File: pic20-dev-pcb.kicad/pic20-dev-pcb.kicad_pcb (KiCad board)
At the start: 2 copper layers, 41.5 x 40.1 mm, 21 parts, among them J1 PGM-Conn, J2 App_Conn_1, J3 App_Conn_2, J4 Conn_SR, J5 Conn_01x03_Male, J6 Conn_BB1, J7 Conn_01x03_Male, SW1 SW_Push, U1 PIC16F1829-IP, U2 TLV1117-33

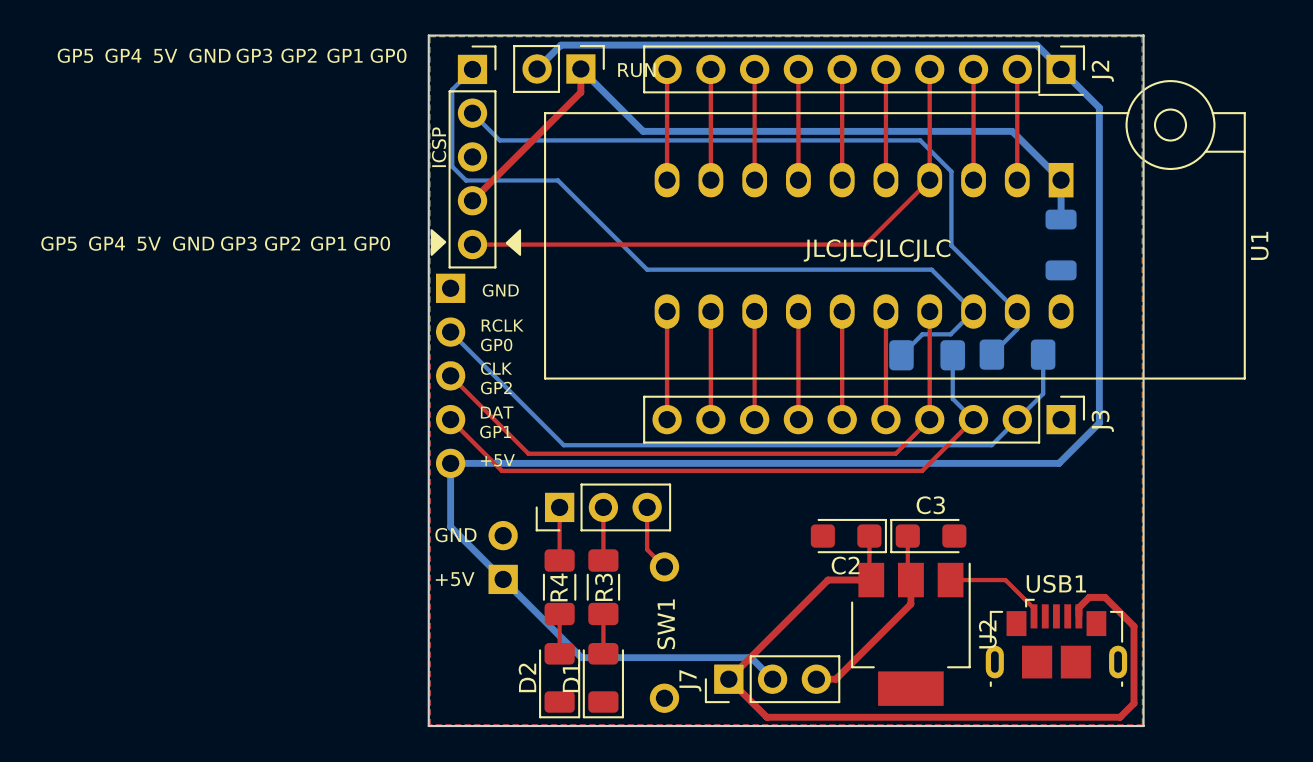
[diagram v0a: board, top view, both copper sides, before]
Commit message: pic20-dev-pcb: Rev 1.2: use DIP-20 footprint for PIC
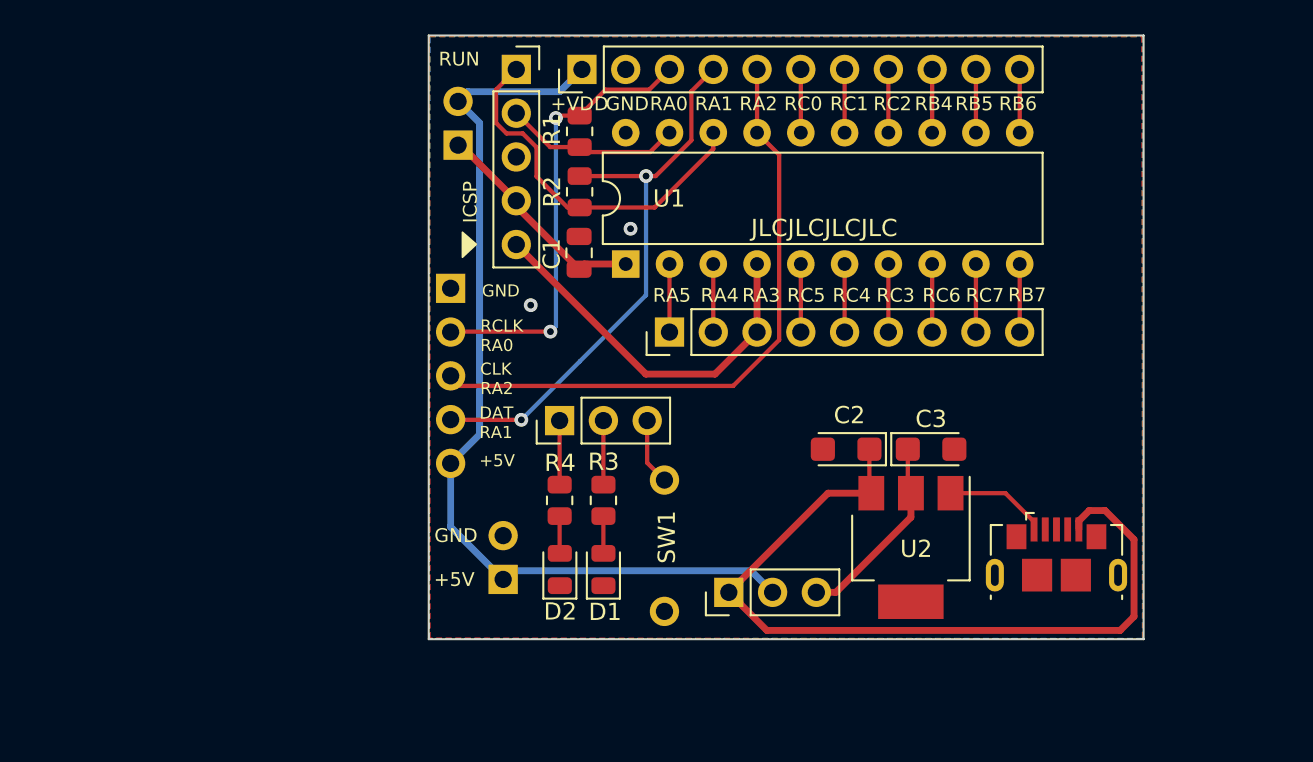
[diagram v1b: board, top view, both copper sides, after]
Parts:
- C1: footprint Capacitor_SMD:C_1206_3216Metric -> Capacitor_SMD:C_0805_2012Metric; moved to F.Cu
- D1, D2: footprint LED_SMD:LED_1206_3216Metric -> LED_SMD:LED_0805_2012Metric
- J2: footprint Connector_PinHeader_2.54mm:PinHeader_1x10_P2.54mm_Vertical -> Connector_PinHeader_2.54mm:PinHeader_1x09_P2.54mm_Vertical
- J3: footprint Connector_PinHeader_2.54mm:PinHeader_1x10_P2.54mm_Vertical -> Connector_PinHeader_2.54mm:PinHeader_1x11_P2.54mm_Vertical
- JP1: moved to B.Cu
- R1, R2: footprint Resistor_SMD:R_1206_3216Metric_Pad1.42x1.75mm_HandSolder -> Resistor_SMD:R_0805_2012Metric; moved to F.Cu
- R3, R4: footprint Resistor_SMD:R_1206_3216Metric_Pad1.30x1.75mm_HandSolder -> Resistor_SMD:R_0805_2012Metric
- U1: footprint Socket:DIP_Socket-20_W4.3_W5.08_W7.62_W10.16_W10.9_3M_220-3342-00-0602J -> Package_DIP:DIP-20_W7.62mm
- moved J3 34.4 mm to (105.4, 76.2), turned to 90 degrees
- moved R1 28.5 mm to (105.3, 79.8), turned to 90 degrees
- moved C1 28.0 mm to (105.2, 86.8), turned to 270 degrees
- moved J2 27.4 mm to (110.5, 91.4), turned to 90 degrees
- moved U1 25.7 mm to (108.0, 87.5), turned to 90 degrees
- moved R2 22.3 mm to (105.3, 83.3), turned to 90 degrees
- moved JP1 8.38 mm to (98.2, 80.6), turned to 0 degrees
- moved D2 6.29 mm to (104.1, 105.2)
- moved D1 6.29 mm to (106.7, 105.2)
- moved J5 5.04 mm to (104.1, 96.6)
- moved J7 5.04 mm to (113.9, 106.5)
- moved U2 5.04 mm to (124.5, 103.9)
- moved C2 5.04 mm to (120.7, 98.2)
- moved C3 5.04 mm to (125.7, 98.2)
- moved R3 5.04 mm to (106.7, 101.2)
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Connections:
- J2 pad 1: /+VDD -> /RA5
- J2 pad 2: /RA5 -> /RA4
- J2 pad 3: /RA4 -> /RA3
- J2 pad 4: /RA3 -> /RC5
- J2 pad 5: /RC5 -> /RC4
- J2 pad 6: /RC4 -> /RC3
- J2 pad 7: /RC3 -> /RC6
- J2 pad 8: /RC6 -> /RC7
- J2 pad 9: /RC7 -> /RB7
- J3 pad 1: GND -> /+VDD
- J3 pad 10: /RB6 -> /RB5
- J3 pad 2: /RA0 -> GND
- J3 pad 3: /RA1 -> /RA0
- J3 pad 4: /RA2 -> /RA1
- J3 pad 5: /RC0 -> /RA2
- J3 pad 6: /RC1 -> /RC0
- J3 pad 7: /RC2 -> /RC1
- J3 pad 8: /RB4 -> /RC2
- J3 pad 9: /RB5 -> /RB4
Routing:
- net /+VDD: track 117.6 -> 54.5 mm
- net Net-(J1-Pad2): track 42.0 -> 10.3 mm
- net Net-(C1-Pad2): track 43.1 -> 13.0 mm
- net Net-(J1-Pad1): track 45.1 -> 21.6 mm
- net /RA0: track 40.6 -> 26.1 mm, vias 0 -> 2
- net /RA3: track 34.5 -> 22.0 mm
- net /RA1: track 37.0 -> 33.8 mm, vias 0 -> 2
- net /RC2: track 6.27 -> 3.67 mm
- net /RC1: track 6.27 -> 3.67 mm
- net /RC0: track 6.27 -> 3.67 mm
- net /RB6: track 6.27 -> 3.67 mm
- net /RB5: track 6.27 -> 3.67 mm
- net /RB4: track 6.27 -> 3.67 mm
- net /RC7: track 6.43 -> 3.95 mm
- net /RC6: track 6.43 -> 3.95 mm
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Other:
- board size 41.5 x 40.1 mm -> 41.5 x 35 mm
- board text added: "+VDD"
- board text added: "CLK RA2"
- board text added: "DAT RA1"
- board text added: "RA0"
- board text added: "RA1"
- board text added: "RA2"
- board text added: "RA3"
- board text added: "RA4"
- board text added: "RA5"
- board text added: "RB4"
- board text added: "RB5"
- board text added: "RB6"
- board text added: "RB7"
- board text added: "RC0"
- board text added: "RC1"
- board text added: "RC2"
- board text added: "RC3"
- board text added: "RC4"
- board text added: "RC5"
- board text added: "RC6"
- board text added: "RC7"
- board text added: "RCLK RA0"
- board text added: "Rev 1.2"
- board text removed: "5V"
- board text removed: "CLK GP2"
- board text removed: "DAT GP1"
- board text removed: "GP0"
- board text removed: "GP1"
- board text removed: "GP2"
- board text removed: "GP3"
- board text removed: "GP4"
- board text removed: "GP5"
- board text removed: "RCLK GP0"
- board text removed: "Rev 6"
- board text removed: "f"

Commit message: pic20-dev-pcb: Rev 1.3: add SPI-connector, use socket for PIC
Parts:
- added J8: SPI_Conn, Connector_PinHeader_2.54mm:PinHeader_1x06_P2.54mm_Vertical, F.Cu at (134.6, 76.2)
- U1: footprint Package_DIP:DIP-20_W7.62mm -> Package_DIP:DIP-20_W7.62mm_Socket
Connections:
- net /RB6 renamed /CLK
- net /RC6 renamed /CS
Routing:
- net /+VDD: track 54.5 -> 84.7 mm
- net /RB4: track 3.67 -> 15.2 mm
- net /CS: track 3.95 -> 15.4 mm
- net /RC7: track 3.95 -> 12.6 mm
- net /CLK: track 3.67 -> 9.41 mm
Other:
- board text added: "CLK"
- board text added: "CS"
- board text added: "Rev 1.3"
- board text added: "SDI"
- board text added: "SDO"
- board text added: "Vdd"
- board text removed: "+VDD"
- board text removed: "Rev 1.2"

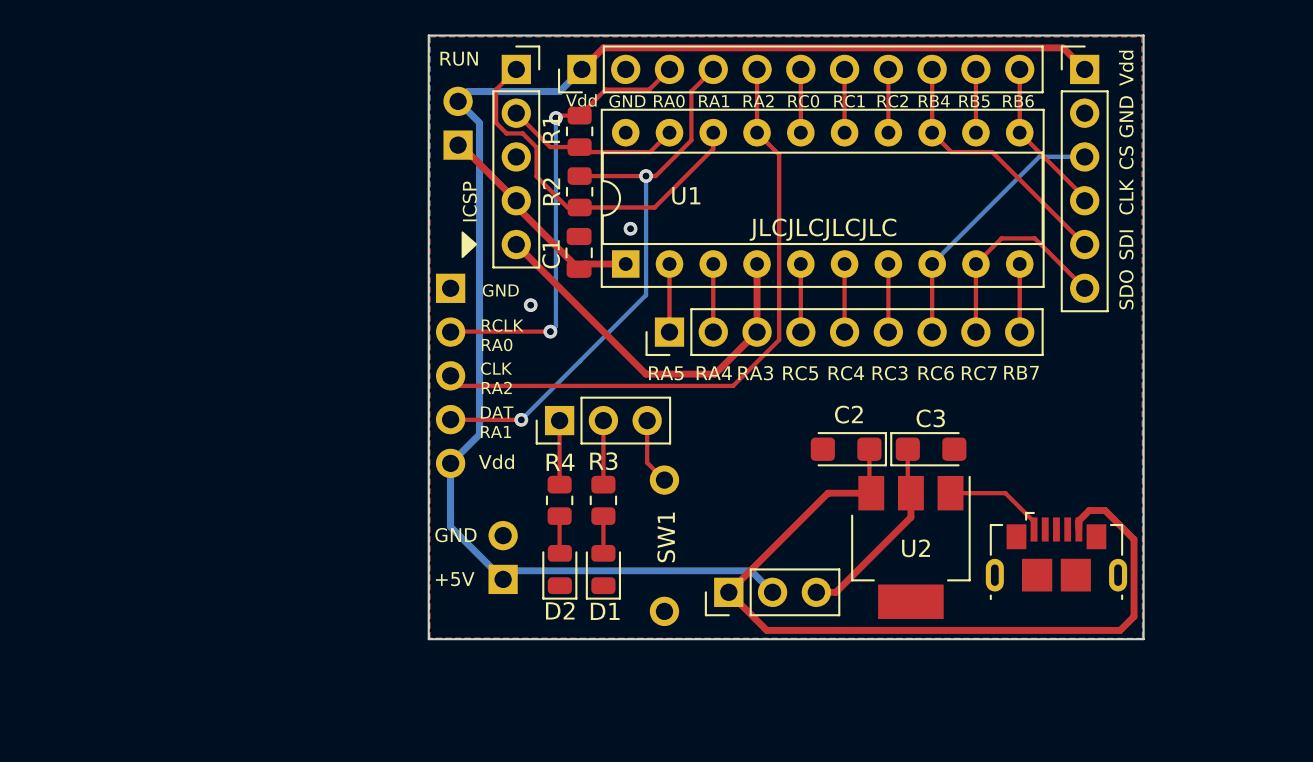
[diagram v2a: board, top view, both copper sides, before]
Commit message: updated footprint for micro-usb
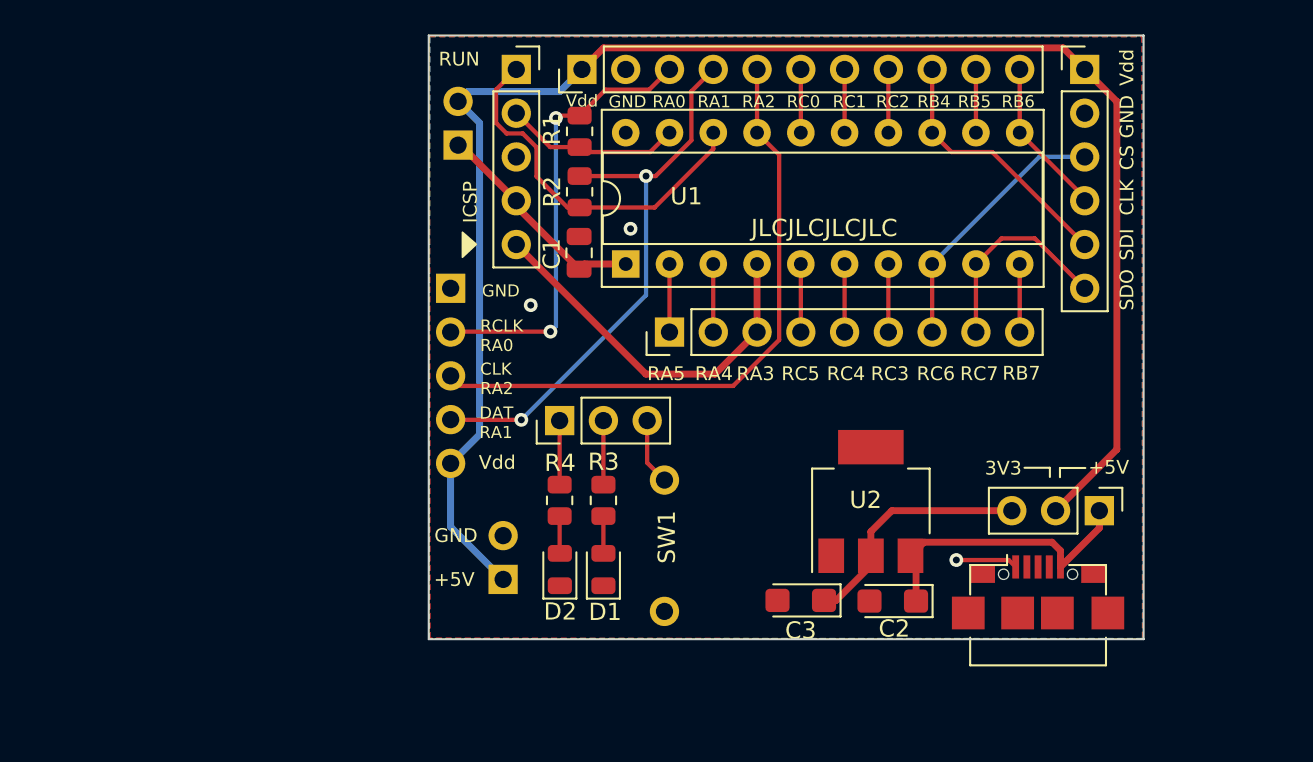
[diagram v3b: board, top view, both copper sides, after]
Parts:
- USB1: footprint Connector_USB:USB_Micro-B_GCT_USB3076-30-A -> user:USB_Micro-B_JLCPCB_40942
- moved J7 22.0 mm to (135.4, 101.8), turned to 270 degrees
- moved C3 11.6 mm to (118.1, 107.0), turned to 180 degrees
- moved C2 9.22 mm to (123.4, 107.0)
- moved U2 3.54 mm to (122.2, 101.3), turned to 90 degrees
- moved USB1 1.29 mm to (131.9, 105.1)
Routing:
- net Net-(C2-Pad1): track 47.1 -> 17.1 mm
- net /+VDD: track 84.7 -> 96.9 mm
- net Net-(C3-Pad1): track 11.5 -> 14.2 mm
- net GND: track 5.98 -> 3.61 mm, vias 2 -> 3
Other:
- board text added: "3V3"
- board text removed: "+"
- board text removed: "-"

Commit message: optimized layout
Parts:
- J4: moved to F.Cu
- moved U2 1.52 mm to (122.0, 99.8)
- moved C2 1.52 mm to (123.3, 105.5)
- moved C3 1.52 mm to (118.0, 105.5)
- moved C1 0.50 mm to (105.2, 87.3)
- moved R2 0.36 mm to (105.1, 83.6)
- moved R1 0.15 mm to (105.1, 79.8)
- turned J4 to 0 degrees
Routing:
- net GND: track 3.61 -> 6.96 mm
- net Net-(C1-Pad2): track 13.0 -> 14.1 mm
- net /RA3: track 22.0 -> 22.7 mm

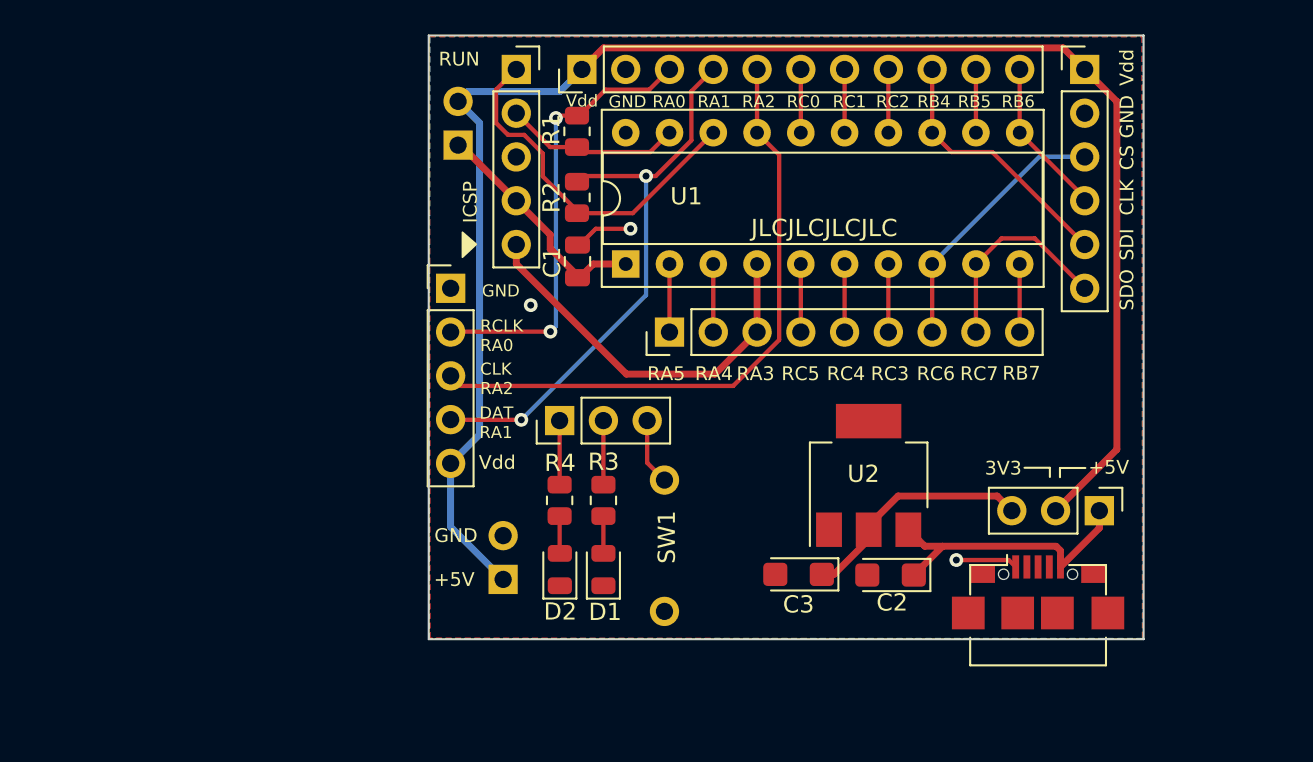
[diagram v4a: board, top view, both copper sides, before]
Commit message: pic20-dev-pcb: Rev 1.4: optimizations, prep for production
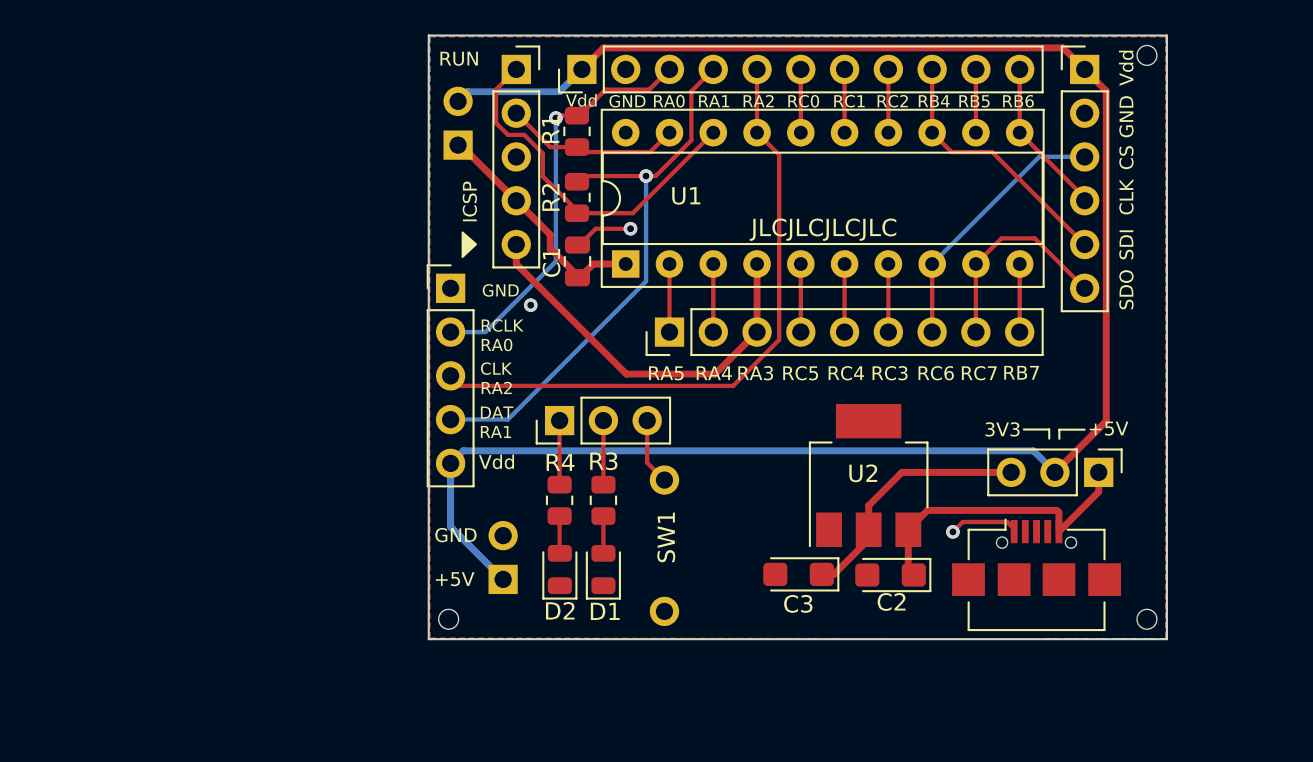
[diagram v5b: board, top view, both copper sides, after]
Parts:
- added REF**: SMT_JLCPCB_ToolingHole, user:SMT_JLCPCB_ToolingHole, F.Cu at (138.2, 108.1)
- added REF**: SMT_JLCPCB_ToolingHole, user:SMT_JLCPCB_ToolingHole, F.Cu at (97.7, 108.1)
- added REF**: SMT_JLCPCB_ToolingHole, user:SMT_JLCPCB_ToolingHole, F.Cu at (138.2, 75.4)
- D1: value LED -> LED yellow
- D2: value LED -> LED red
- R3, R4: value 1kΩ -> 1K
- moved J7 2.22 mm to (135.4, 99.6)
- moved USB1 0.66 mm to (131.8, 104.4)
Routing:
- net /+VDD: track 96.9 -> 107.9 mm
- net /RA0: track 26.1 -> 23.9 mm, vias 2 -> 1
- net Net-(C3-Pad1): track 13.7 -> 14.8 mm
- net /RA1: track 34.0 -> 33.4 mm, vias 2 -> 1
- net Net-(C2-Pad1): track 16.8 -> 17.4 mm
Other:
- board size 41.5 x 35 mm -> 42.8 x 35 mm
- board text added: "Rev 1.4"
- board text removed: "Rev 1.3"

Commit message: Rev 1.5: bugfix Micro-USB connector
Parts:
- USB1: value Micro-USB_Breakout -> Micro-USB
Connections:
- USB1 pad 1: GND -> Net-(C2-Pad1)
- USB1 pad 5: Net-(C2-Pad1) -> GND
- USB1 pad 6: (no net) -> GND
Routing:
- net Net-(C2-Pad1): track 17.4 -> 15.8 mm
- net GND: track 7.30 -> 6.13 mm, vias 3 -> 2
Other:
- board text added: "Rev 1.5"
- board text removed: "Rev 1.4"
